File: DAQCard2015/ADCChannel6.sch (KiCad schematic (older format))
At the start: 50 parts, among them U10 LTC6403, U6 LTC6403, U7 AD9219, U8 LTC6403, U9 LTC6403

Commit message: Replaces single ample with 4-channel varients. Greatly reducing part count
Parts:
- removed C23, C33, C37, C38: .01uF, symbol C
- removed C24, C25, C29, C31, C32: .1uF, symbol C
- removed C26, C27, C28, C34, C35, C36, C39, C40, C41, C42, C43, C44: C, symbol C
- removed C30: 2.2uF, symbol CP
- removed R25, R32, R37, R38: Rt, symbol R
- removed R26, R27, R33, R34, R39, R40, R41, R42: Ri, symbol R
- removed R29, R30, R35, R36, R43, R44, R45, R46: Rf, symbol R
- removed R31: 10k, symbol R
- removed R47: 2.7k, symbol R
- removed R48: 1k, symbol R
- removed U10, U6, U8, U9: LTC6403, symbol LTC6403
- removed U7: AD9219, symbol AD9219
- added C72, C73, C74: C, symbol C
- added C75: .01uF, symbol C
- added C76, C77, C78, C80, C81: .1uF, symbol C
- added C79: 2.2uF, symbol CP
- added R53, R54, R55, R56: Rt, symbol R
- added R57: 2.7k, symbol R
- added R58: 1k, symbol R
- added R59: 10k, symbol R
- added RP22: R_PACK8, symbol R_PACK8
- added RP23, RP24: Rf, symbol R_PACK4
- added U16: THS4524IDBTR, symbol THS4524IDBTR
- added U17: AD9219, symbol AD9219
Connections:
- net labels added: 3V3ana, VOCM
- net labels removed: 18ana, 3V3, Vocm
- wire segments 178 -> 192
- no-connect marks 12 -> 4
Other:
- note removed: "100R Termination \nis common for all ADCs."

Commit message: Finishes initial version of schematic(mostly). And adds a whole bunch of new footprints!
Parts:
- removed C74: C, symbol C
- removed C75: .01uF, symbol C
- removed C76, C77, C78, C80, C81: .1uF, symbol C
- removed C79: 2.2uF, symbol CP
- added C65: 10uF, extras:SMD_Cap_3mmDia, symbol CP
- added C66, C68, C69, C70: .1uF, Capacitors_SMD:C_0603, symbol C
- added C67: .01uF, Capacitors_SMD:C_0603, symbol C
- added C71: 2.2uF, extras:SMD_Cap_3mmDia, symbol CP
- C72, C73: value C -> .1uF; footprint (none) -> Capacitors_SMD:C_0603
- R53, R54, R55, R56, R57, R58, R59: footprint (none) -> Resistors_SMD:R_0603
- RP22: footprint (none) -> extras:R8_MNR18
- RP23, RP24: footprint (none) -> extras:R4-MNR04
- U16: footprint (none) -> Housings_SSOP:TSSOP-38_4.4x9.7mm_Pitch0.5mm
- U17: footprint (none) -> SMD_Packages:QFN-48-1EP
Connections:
- net 3V3ana: now also C65.1, C66.1; no longer C72.1, C73.1
- net ADC_CLK+: now also C69.2
- net ADC_CLK-: now also C68.2
- net GNDana: now also C73.1, C65.2, C66.2, C67.2, C70.2; no longer C72.2, C73.2
- net VOCM: now also C67.1
- net at U17.43 (REFB): now also C72.1, C73.2, C71.2
- net at U17.44 (REFT): now also C72.2, C70.1, C71.1
- net at U17.7 (CLK-): now also C68.1
- net at U17.8 (CLK+): now also C69.1
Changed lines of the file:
@@
 $Comp
 L AD9219 U17
-U 1 1 55C488DE
+U 1 1 55CB5753
 P 9050 3700
 F 0 "U17" H 8250 4650 60  0000 C CNN
 F 1 "AD9219" H 9050 3800 60  0000 C CNN
-F 2 "" H 8650 3700 60  0000 C CNN
+F 2 "SMD_Packages:QFN-48-1EP" H 8650 3700 60  0001 C CNN
 F 3 "" H 8650 3700 60  0000 C CNN
 	1    9050 3700
@@
 $Comp
 L R R57
-U 1 1 55CFF5F4
+U 1 1 55CB5788
 P 3350 6700
 F 0 "R57" V 3430 6700 50  0000 C CNN
 F 1 "2.7k" V 3350 6700 50  0000 C CNN
-F 2 "" V 3280 6700 30  0000 C CNN
+F 2 "Resistors_SMD:R_0603" V 3280 6700 30  0001 C CNN
 F 3 "" H 3350 6700 30  0000 C CNN
 	1    3350 6700
@@
 $Comp
 L R R58
-U 1 1 55CFF5E0
+U 1 1 55CB5778
 P 3350 7100
 F 0 "R58" V 3430 7100 50  0000 C CNN
 F 1 "1k" V 3350 7100 50  0000 C CNN
-F 2 "" V 3280 7100 30  0000 C CNN
+F 2 "Resistors_SMD:R_0603" V 3280 7100 30  0001 C CNN
 F 3 "" H 3350 7100 30  0000 C CNN
 	1    3350 7100
@@
 Must terminate with 100R!
 $Comp
-L C C72
-U 1 1 55CFF5CB
-P 2650 6900
-F 0 "C72" H 2675 7000 50  0000 L CNN
-F 1 "C" H 2675 6800 50  0000 L CNN
-F 2 "" H 2688 6750 30  0000 C CNN
-F 3 "" H 2650 6900 60  0000 C CNN
-	1    2650 6900
-	1    0    0    -1
-$EndComp
-$Comp
-L C C73
-U 1 1 55C4E800
-P 2850 6900
-F 0 "C73" H 2875 7000 50  0000 L CNN
-F 1 "C" H 2875 6800 50  0000 L CNN
-F 2 "" H 2888 6750 30  0000 C CNN
-F 3 "" H 2850 6900 60  0000 C CNN
-	1    2850 6900
-	1    0    0    -1
-$EndComp
-$Comp
-L C C74
-U 1 1 55CFF5BC
+L C C66
+U 1 1 55CB575F
 P 3050 6900
-F 0 "C74" H 3075 7000 50  0000 L CNN
-F 1 "C" H 3075 6800 50  0000 L CNN
-F 2 "" H 3088 6750 30  0000 C CNN
+F 0 "C66" H 3075 7000 50  0000 L CNN
+F 1 ".1uF" H 3050 6800 50  0000 L CNN
+F 2 "Capacitors_SMD:C_0603" H 3088 6750 30  0001 C CNN
 F 3 "" H 3050 6900 60  0000 C CNN
 	1    3050 6900
@@
 ADC_SCLK
 $Comp
-L C C76
-U 1 1 55CFF5C2
+L C C68
+U 1 1 55CB5762
 P 7550 3650
-F 0 "C76" H 7575 3750 50  0000 L CNN
+F 0 "C68" H 7575 3750 50  0000 L CNN
 F 1 ".1uF" H 7575 3550 50  0000 L CNN
-F 2 "" H 7588 3500 30  0000 C CNN
+F 2 "Capacitors_SMD:C_0603" H 7588 3500 30  0001 C CNN
 F 3 "" H 7550 3650 60  0000 C CNN
 	1    7550 3650
@@
 $EndComp
 $Comp
-L C C77
-U 1 1 55CFF5E5
+L C C69
+U 1 1 55CE4061
 P 7550 3950
-F 0 "C77" H 7575 4050 50  0000 L CNN
+F 0 "C69" H 7575 4050 50  0000 L CNN
 F 1 ".1uF" H 7575 3850 50  0000 L CNN
-F 2 "" H 7588 3800 30  0000 C CNN
+F 2 "Capacitors_SMD:C_0603" H 7588 3800 30  0001 C CNN
 F 3 "" H 7550 3950 60  0000 C CNN
 	1    7550 3950
@@
 DCO+
 $Comp
-L C C81
-U 1 1 55CFF5F8
+L C C73
+U 1 1 55CB578E
 P 9300 1750
-F 0 "C81" H 9325 1850 50  0000 L CNN
+F 0 "C73" H 9325 1850 50  0000 L CNN
 F 1 ".1uF" H 9325 1650 50  0000 L CNN
-F 2 "" H 9338 1600 30  0000 C CNN
+F 2 "Capacitors_SMD:C_0603" H 9338 1600 30  0001 C CNN
 F 3 "" H 9300 1750 60  0000 C CNN
 	1    9300 1750
@@
 $EndComp
 $Comp
-L C C78
-U 1 1 55CFF5D1
+L C C70
+U 1 1 55CB576E
 P 8600 1750
-F 0 "C78" H 8625 1850 50  0000 L CNN
+F 0 "C70" H 8625 1850 50  0000 L CNN
 F 1 ".1uF" H 8625 1650 50  0000 L CNN
-F 2 "" H 8638 1600 30  0000 C CNN
+F 2 "Capacitors_SMD:C_0603" H 8638 1600 30  0001 C CNN
 F 3 "" H 8600 1750 60  0000 C CNN
 	1    8600 1750
@@
 $EndComp
 $Comp
-L C C80
-U 1 1 55CFF5D9
+L C C72
+U 1 1 55CB5773
 P 8950 1650
-F 0 "C80" H 8975 1750 50  0000 L CNN
+F 0 "C72" H 8975 1750 50  0000 L CNN
 F 1 ".1uF" H 8975 1550 50  0000 L CNN
-F 2 "" H 8988 1500 30  0000 C CNN
+F 2 "Capacitors_SMD:C_0603" H 8988 1500 30  0001 C CNN
 F 3 "" H 8950 1650 60  0000 C CNN
 	1    8950 1650
@@
 GNDana
 $Comp
-L CP C79
-U 1 1 55CFF5FF
+L CP C71
+U 1 1 55CB5795
 P 8950 1450
-F 0 "C79" H 8975 1550 50  0000 L CNN
+F 0 "C71" H 8975 1550 50  0000 L CNN
 F 1 "2.2uF" H 8975 1350 50  0000 L CNN
-F 2 "" H 8988 1300 30  0000 C CNN
+F 2 "extras:SMD_Cap_3mmDia" H 8988 1300 30  0001 C CNN
 F 3 "" H 8950 1450 60  0000 C CNN
 	1    8950 1450
@@
 $Comp
 L R R59
-U 1 1 55CFF5EA
+U 1 1 55CB577D
 P 9900 1950
 F 0 "R59" V 9980 1950 50  0000 C CNN
 F 1 "10k" V 9900 1950 50  0000 C CNN
-F 2 "" V 9830 1950 30  0000 C CNN
+F 2 "Resistors_SMD:R_0603" V 9830 1950 30  0001 C CNN
 F 3 "" H 9900 1950 30  0000 C CNN
 	1    9900 1950
@@
 $Comp
 L THS4524IDBTR U16
-U 1 1 55CFF60A
+U 1 1 55CB579E
 P 4400 3700
 F 0 "U16" H 4700 2750 60  0000 C CNN
 F 1 "THS4524IDBTR" H 4400 4850 60  0000 C CNN
-F 2 "" H 4600 3800 60  0000 C CNN
+F 2 "Housings_SSOP:TSSOP-38_4.4x9.7mm_Pitch0.5mm" H 4600 3800 60  0001 C CNN
 F 3 "" H 4600 3800 60  0000 C CNN
 	1    4400 3700
@@
 $EndComp
 $Comp
-L C C75
-U 1 1 55CFF611
+L C C67
+U 1 1 55CB57A6
 P 3600 7100
-F 0 "C75" H 3625 7200 50  0000 L CNN
+F 0 "C67" H 3625 7200 50  0000 L CNN
 F 1 ".01uF" H 3625 7000 50  0000 L CNN
-F 2 "" H 3638 6950 30  0000 C CNN
+F 2 "Capacitors_SMD:C_0603" H 3638 6950 30  0001 C CNN
 F 3 "" H 3600 7100 60  0000 C CNN
 	1    3600 7100
@@
 Connection ~ 3600 6900
 Wire Wire Line
-	2650 6500 3750 6500
-Wire Wire Line
 	3050 6500 3050 6750
 Connection ~ 3350 6500
@@
 Connection ~ 3050 6500
 Wire Wire Line
-	2650 6500 2650 6750
-Connection ~ 2850 6500
-Wire Wire Line
-	2650 7300 3750 7300
-Wire Wire Line
 	3050 7300 3050 7050
 Wire Wire Line
 	2850 7300 2850 7050
 Connection ~ 3050 7300
-Wire Wire Line
-	2650 7300 2650 7050
-Connection ~ 2850 7300
 Wire Wire Line
 	3600 7300 3600 7250
@@
 $Comp
 L R R56
-U 1 1 55CFF614
+U 1 1 55CB57A9
 P 1850 4350
 F 0 "R56" V 1930 4350 50  0000 C CNN
 F 1 "Rt" V 1850 4350 50  0000 C CNN
-F 2 "" V 1780 4350 30  0000 C CNN
+F 2 "Resistors_SMD:R_0603" V 1780 4350 30  0001 C CNN
 F 3 "" H 1850 4350 30  0000 C CNN
 	1    1850 4350
@@
 $Comp
 L R R55
-U 1 1 55CFF621
+U 1 1 55CB57B2
 P 1850 3850
 F 0 "R55" V 1930 3850 50  0000 C CNN
 F 1 "Rt" V 1850 3850 50  0000 C CNN
-F 2 "" V 1780 3850 30  0000 C CNN
+F 2 "Resistors_SMD:R_0603" V 1780 3850 30  0001 C CNN
 F 3 "" H 1850 3850 30  0000 C CNN
 	1    1850 3850
@@
 $Comp
 L R R54
-U 1 1 55CFF624
+U 1 1 55CB57BA
 P 1850 3350
 F 0 "R54" V 1930 3350 50  0000 C CNN
 F 1 "Rt" V 1850 3350 50  0000 C CNN
-F 2 "" V 1780 3350 30  0000 C CNN
+F 2 "Resistors_SMD:R_0603" V 1780 3350 30  0001 C CNN
 F 3 "" H 1850 3350 30  0000 C CNN
 	1    1850 3350
@@
 $Comp
 L R R53
-U 1 1 55CFF62B
+U 1 1 55CB57C1
 P 1850 2850
 F 0 "R53" V 1930 2850 50  0000 C CNN
 F 1 "Rt" V 1850 2850 50  0000 C CNN
-F 2 "" V 1780 2850 30  0000 C CNN
+F 2 "Resistors_SMD:R_0603" V 1780 2850 30  0001 C CNN
 F 3 "" H 1850 2850 30  0000 C CNN
 	1    1850 2850
@@
 $Comp
 L R_PACK4 RP23
-U 1 1 55CFF633
+U 1 1 55CB57C7
 P 4250 5150
 F 0 "RP23" H 4250 5600 50  0000 C CNN
 F 1 "Rf" H 4250 5100 50  0000 C CNN
-F 2 "" H 4250 5150 60  0000 C CNN
+F 2 "extras:R4-MNR04" H 4250 5150 60  0001 C CNN
 F 3 "" H 4250 5150 60  0000 C CNN
 	1    4250 5150
@@
 $Comp
 L R_PACK4 RP24
-U 1 1 55CFF63C
+U 1 1 55CB5751
 P 4300 2450
 F 0 "RP24" H 4300 2900 50  0000 C CNN
 F 1 "Rf" H 4300 2400 50  0000 C CNN
-F 2 "" H 4300 2450 60  0000 C CNN
+F 2 "extras:R4-MNR04" H 4300 2450 60  0001 C CNN
 F 3 "" H 4300 2450 60  0000 C CNN
 	1    4300 2450
@@
 $Comp
 L R_PACK8 RP22
-U 1 1 55CFF643
+U 1 1 55CFF641
 P 2750 3600
 F 0 "RP22" H 2750 4050 50  0000 C CNN
 F 1 "R_PACK8" H 2750 3150 50  0000 C CNN
-F 2 "" H 2750 3600 60  0000 C CNN
+F 2 "extras:R8_MNR18" H 2750 3600 60  0001 C CNN
 F 3 "" H 2750 3600 60  0000 C CNN
 	1    2750 3600
@@
 Text GLabel 10150 1950 2    40   Input ~ 0
 GNDana
+Wire Wire Line
+	3750 6500 2850 6500
+Wire Wire Line
+	2850 7300 3750 7300
+$Comp
+L CP C65
+U 1 1 55CB5743
+P 2850 6900
+F 0 "C65" H 2875 7000 50  0000 L CNN
+F 1 "10uF" H 2850 6800 50  0000 L CNN
+F 2 "extras:SMD_Cap_3mmDia" H 2888 6750 30  0001 C CNN
+F 3 "" H 2850 6900 60  0000 C CNN
+	1    2850 6900
+	1    0    0    -1
+$EndComp
 $EndSCHEMATC

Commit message: Adds a more-or-less complete BOM to DAQ Card
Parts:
- C67: value .01uF -> 10000pF
- RP22: value R_PACK8 -> Ri
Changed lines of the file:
@@
 $Descr A4 11693 8268
 encoding utf-8
-Sheet 3 13
+Sheet 10 13
 Title ""
 Date ""
@@
 P 3600 7100
 F 0 "C67" H 3625 7200 50  0000 L CNN
-F 1 ".01uF" H 3625 7000 50  0000 L CNN
+F 1 "10000pF" H 3625 7000 50  0000 L CNN
 F 2 "Capacitors_SMD:C_0603" H 3638 6950 30  0001 C CNN
 F 3 "" H 3600 7100 60  0000 C CNN
@@
 P 2750 3600
 F 0 "RP22" H 2750 4050 50  0000 C CNN
-F 1 "R_PACK8" H 2750 3150 50  0000 C CNN
+F 1 "Ri" H 2750 3150 50  0000 C CNN
 F 2 "extras:R8_MNR18" H 2750 3600 60  0001 C CNN
 F 3 "" H 2750 3600 60  0000 C CNN

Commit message: Updates to DAQCard2015, especially to power systems
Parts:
- C65, C71: footprint extras:SMD_Cap_3mmDia -> Capacitors_SMD:C_0805
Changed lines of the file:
@@
 F 0 "C71" H 8975 1550 50  0000 L CNN
 F 1 "2.2uF" H 8975 1350 50  0000 L CNN
-F 2 "extras:SMD_Cap_3mmDia" H 8988 1300 30  0001 C CNN
+F 2 "Capacitors_SMD:C_0805" H 8988 1300 30  0001 C CNN
 F 3 "" H 8950 1450 60  0000 C CNN
 	1    8950 1450
@@
 F 0 "C65" H 2875 7000 50  0000 L CNN
 F 1 "10uF" H 2850 6800 50  0000 L CNN
-F 2 "extras:SMD_Cap_3mmDia" H 2888 6750 30  0001 C CNN
+F 2 "Capacitors_SMD:C_0805" H 2888 6750 30  0001 C CNN
 F 3 "" H 2850 6900 60  0000 C CNN
 	1    2850 6900

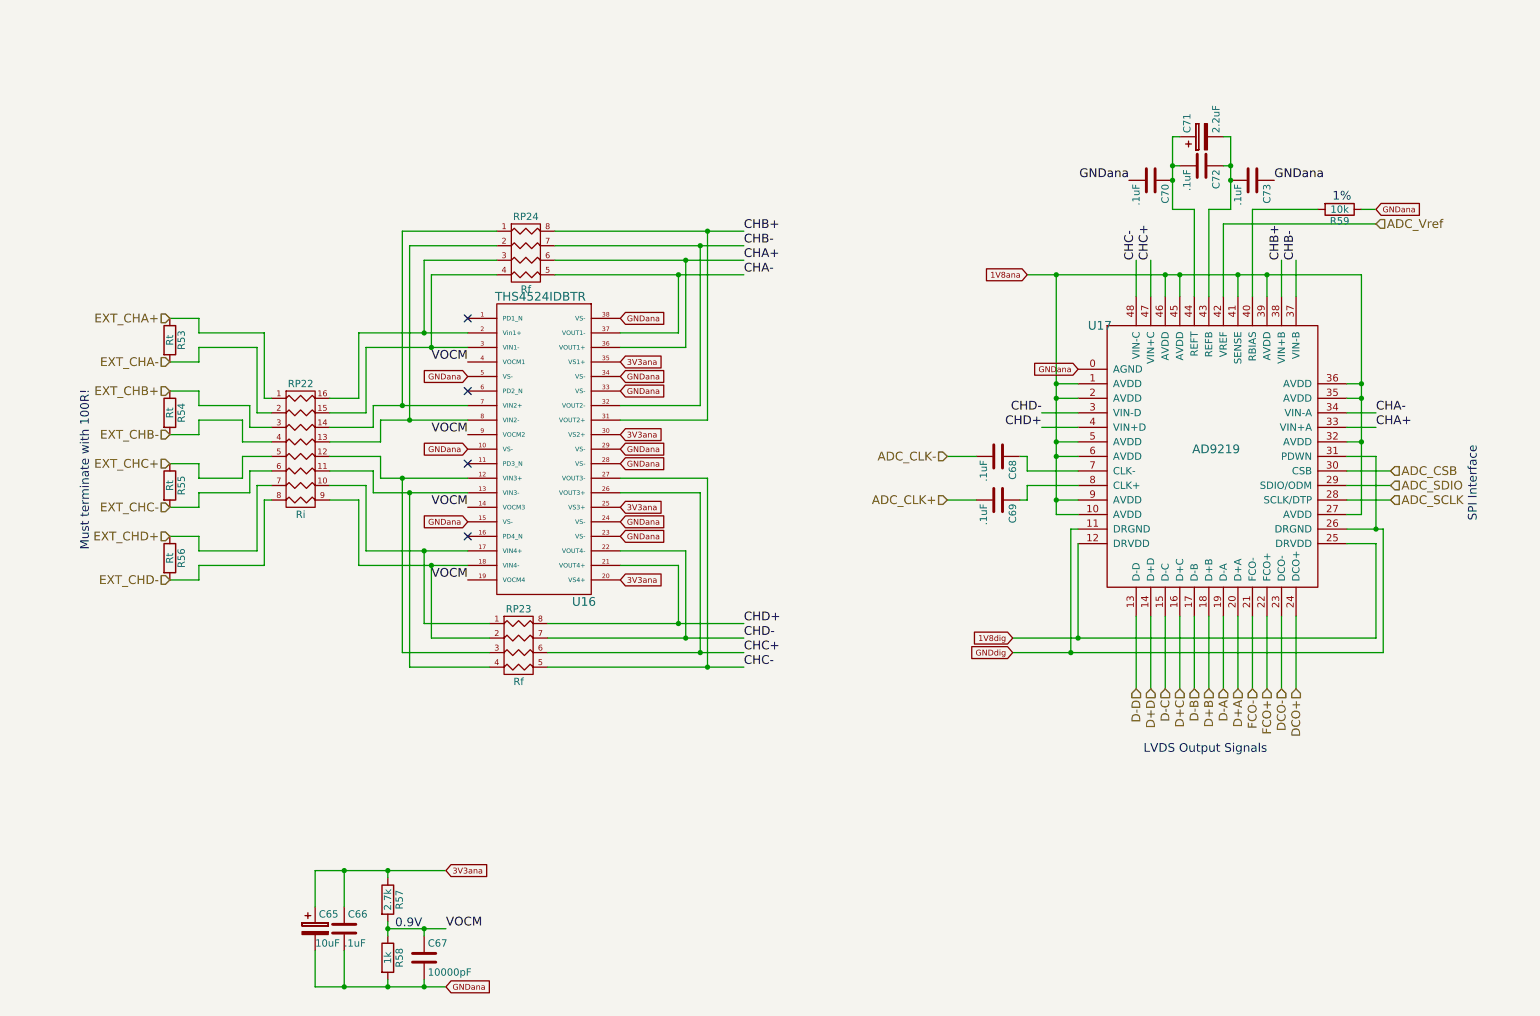
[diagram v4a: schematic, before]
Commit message: propogate previous changes to other channels and schematic
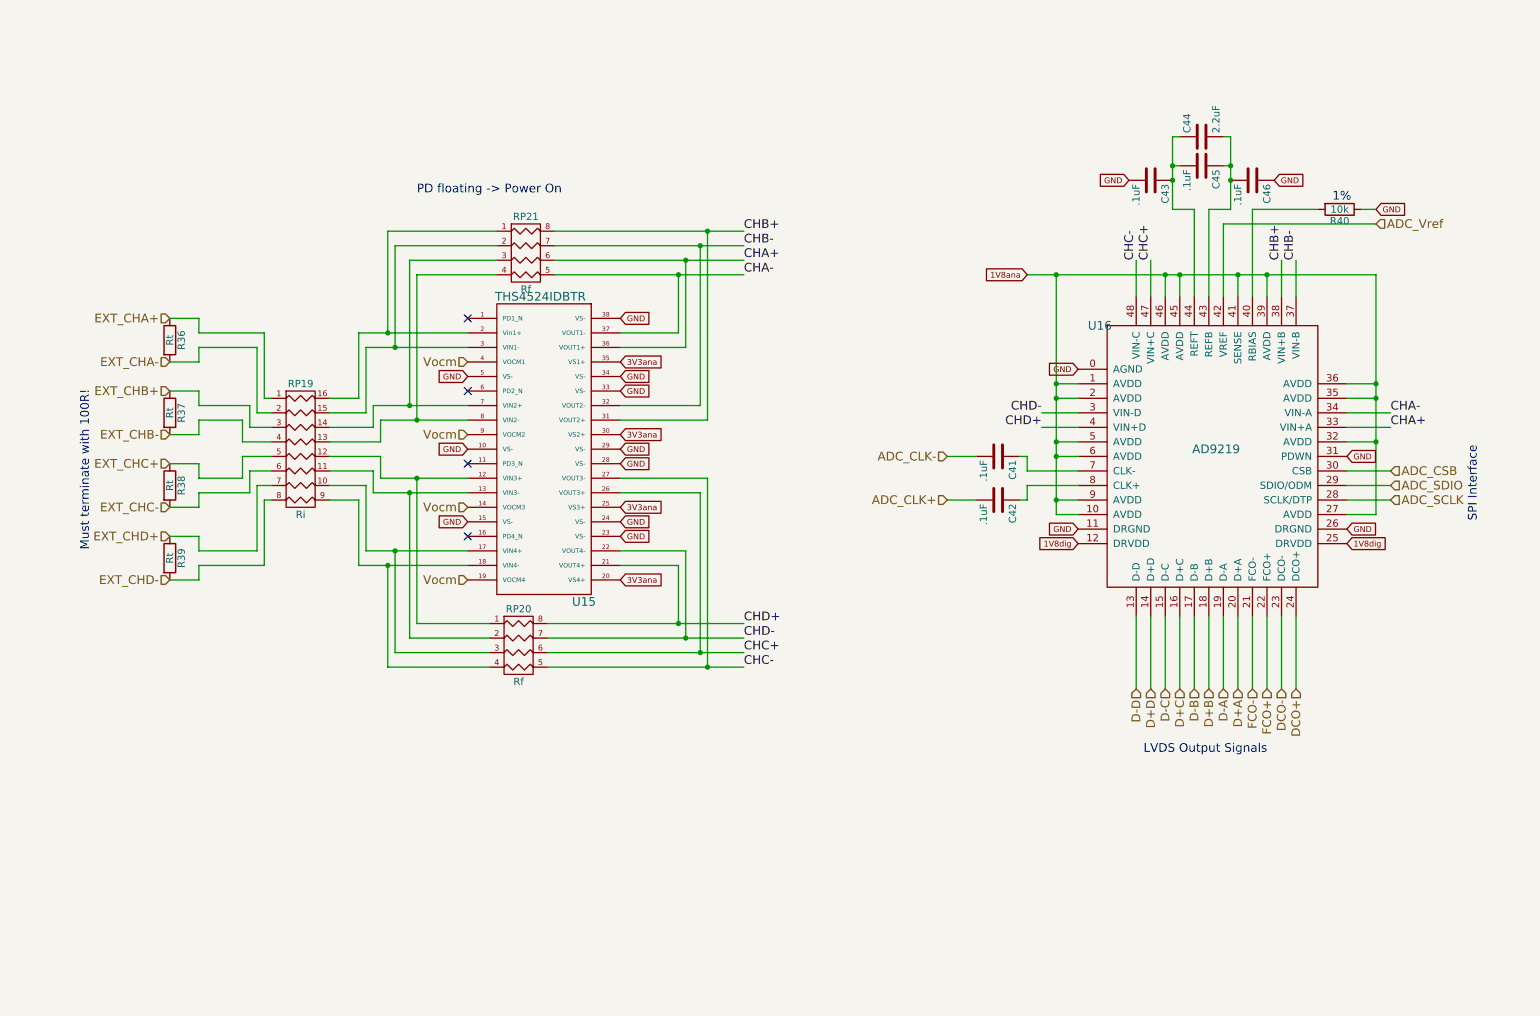
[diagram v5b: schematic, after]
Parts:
- removed C65: 10uF, Capacitors_SMD:C_0805, symbol CP
- removed C66, C68, C69, C70, C72, C73: .1uF, Capacitors_SMD:C_0603, symbol C
- removed C67: 10000pF, Capacitors_SMD:C_0603, symbol C
- removed C71: 2.2uF, Capacitors_SMD:C_0805, symbol CP
- removed R53, R54, R55, R56: Rt, Resistors_SMD:R_0603, symbol R
- removed R57: 2.7k, Resistors_SMD:R_0603, symbol R
- removed R58: 1k, Resistors_SMD:R_0603, symbol R
- removed R59: 10k, Resistors_SMD:R_0603, symbol R
- removed RP22: Ri, extras:R8_MNR18, symbol R_PACK8
- removed RP23, RP24: Rf, extras:R4-MNR04, symbol R_PACK4
- removed U16: THS4524IDBTR, Housings_SSOP:TSSOP-38_4.4x9.7mm_Pitch0.5mm, symbol THS4524IDBTR
- removed U17: AD9219, SMD_Packages:QFN-48-1EP, symbol AD9219
- added C41, C42, C43, C45, C46: .1uF, Capacitors_SMD:C_0603, symbol C
- added C44: 2.2uF, Capacitors_SMD:C_0805, symbol C
- added R36, R37, R38, R39: Rt, Resistors_SMD:R_0603, symbol R
- added R40: 10k, Resistors_SMD:R_0603, symbol R
- added RP19: Ri, extras:R8_MNR18, symbol R_PACK8
- added RP20, RP21: Rf, extras:R4-MNR04, symbol R_PACK4
- added U15: THS4524IDBTR, Housings_SSOP:TSSOP-38_4.4x9.7mm_Pitch0.5mm, symbol THS4524IDBTR
- added U16: AD9219, extras:QFN-48-1EP, symbol AD9219
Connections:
- net 1V8ana: now also U16.1 (AVDD), U16.10 (AVDD), U16.2 (AVDD), U16.27 (AVDD), U16.32 (AVDD), U16.35 (AVDD), U16.36 (AVDD), U16.39 (AVDD), U16.41 (SENSE), U16.45 (AVDD), U16.46 (AVDD), U16.5 (AVDD), U16.6 (AVDD), U16.9 (AVDD)
- net 1V8dig: now also U16.12 (DRVDD), U16.25 (DRVDD)
- net 3V3ana: now also U15.20 (VS4+), U15.25 (VS3+), U15.30 (VS2+), U15.35 (VS1+)
- net ADC_CLK+: now also C42.2
- net ADC_CLK-: now also C41.2
- net ADC_CSB: now also U16.30 (CSB)
- net ADC_SCLK: now also U16.28 (SCLK/DTP)
- net ADC_SDIO: now also U16.29 (SDIO/ODM)
- net ADC_Vref: now also U16.42 (VREF)
- net CHA+: now also RP21.6 (R3), U15.36 (VOUT1+), U16.33 (VIN+A)
- net CHA-: now also RP21.5 (R4), U15.37 (VOUT1-), U16.34 (VIN-A)
- net CHB+: now also RP21.8 (R1), U15.31 (VOUT2+), U16.38 (VIN+B)
- net CHB-: now also RP21.7 (R2), U15.32 (VOUT2-), U16.37 (VIN-B)
- net CHC+: now also RP20.6 (R3), U15.26 (VOUT3+), U16.47 (VIN+C)
- net CHC-: now also RP20.5 (R4), U15.27 (VOUT3-), U16.48 (VIN-C)
- net CHD+: now also RP20.8 (R1), U15.21 (VOUT4+), U16.4 (VIN+D)
- net CHD-: now also RP20.7 (R2), U15.22 (VOUT4-), U16.3 (VIN-D)
- net D+A: now also U16.20 (D+A)
- net D+B: now also U16.18 (D+B)
- net D+C: now also U16.16 (D+C)
- net D+D: now also U16.14 (D+D)
- net D-A: now also U16.19 (D-A)
- net D-B: now also U16.17 (D-B)
- net D-C: now also U16.15 (D-C)
- net D-D: now also U16.13 (D-D)
- net DCO+: now also U16.24 (DCO+)
- net DCO-: now also U16.23 (DCO-)
- net EXT_CHA+: now also R36.1, RP19.1 (P1)
- net EXT_CHA-: now also R36.2, RP19.2 (P2)
- net EXT_CHB+: now also R37.1, RP19.3 (P3)
- net EXT_CHB-: now also R37.2, RP19.4 (P4)
- net EXT_CHC+: now also R38.1, RP19.5 (P5)
- net EXT_CHC-: now also R38.2, RP19.6 (P6)
- net EXT_CHD+: now also R39.1, RP19.7 (P7)
- net EXT_CHD-: now also R39.2, RP19.8 (P8)
- net FCO+: now also U16.22 (FCO+)
- net FCO-: now also U16.21 (FCO-)
- new net: RP19.16 (R1), RP21.1 (P1), U15.2 (Vin1+)
- new net: RP19.15 (R2), RP21.2 (P2), U15.3 (VIN1-)
- new net: RP19.14 (R3), RP21.3 (P3), U15.7 (VIN2+)
- new net: RP19.13 (R4), RP21.4 (P4), U15.8 (VIN2-)
- new net: R40.2, U16.40 (RBIAS)
- new net: C42.1, U16.8 (CLK+)
- new net: C44.2, C45.1, C46.2, U16.43 (REFB)
- new net: C43.1, C44.1, C45.2, U16.44 (REFT)
- new net: C41.1, U16.7 (CLK-)
- new net: RP19.12 (R5), RP20.1 (P1), U15.12 (VIN3+)
- new net: RP19.11 (R6), RP20.2 (P2), U15.13 (VIN3-)
- new net: RP19.10 (R7), RP20.3 (P3), U15.17 (VIN4+)
- new net: RP19.9 (R8), RP20.4 (P4), U15.18 (VIN4-)
- new net GND: C43.2, C46.1, R40.1, U15.10 (VS-), U15.15 (VS-), U15.23 (VS-), U15.24 (VS-), U15.28 (VS-), U15.29 (VS-), U15.33 (VS-), U15.34 (VS-), U15.38 (VS-), U15.5 (VS-), U16.0 (AGND), U16.11 (DRGND), U16.26 (DRGND), U16.31 (PDWN)
- new net Vocm: U15.14 (VOCM3), U15.19 (VOCM4), U15.4 (VOCM1), U15.9 (VOCM2)
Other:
- note added: "PD floating -> Power On"
- note removed: "0.9V"

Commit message: Various updates to DAQ board focusing on power system
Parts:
- U15: footprint Housings_SSOP:TSSOP-38_4.4x9.7mm_Pitch0.5mm -> extras:TSSOP-38_4.4x9.7mm_Pitch0.5mm
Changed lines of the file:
@@
 F 0 "U15" H 4700 2750 60  0000 C CNN
 F 1 "THS4524IDBTR" H 4400 4850 60  0000 C CNN
-F 2 "Housings_SSOP:TSSOP-38_4.4x9.7mm_Pitch0.5mm" H 4600 3800 60  0001 C CNN
+F 2 "extras:TSSOP-38_4.4x9.7mm_Pitch0.5mm" H 4600 3800 60  0001 C CNN
 F 3 "" H 4600 3800 60  0000 C CNN
 	1    4400 3700
